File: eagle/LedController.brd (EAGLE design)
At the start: 64.8 x 34.3 mm, 20 parts, among them IC2 MEGA8-P, IC3 7805, Q1 16MHz, Q2 FDS8884, Q3 FDS8884, Q4 FDS8884, X1 2510-, X2 MKDSN1,5/4-5,08

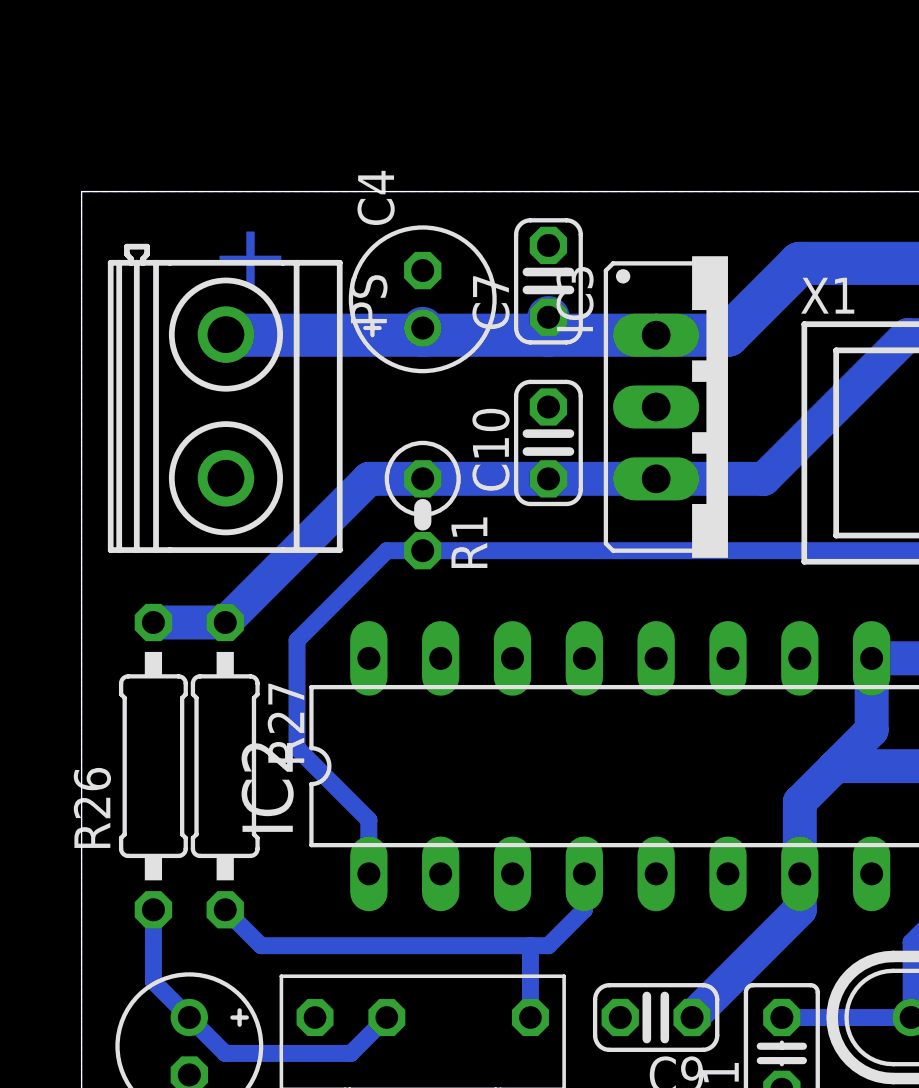
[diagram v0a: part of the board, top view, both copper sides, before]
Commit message: Add reverse polarity protection
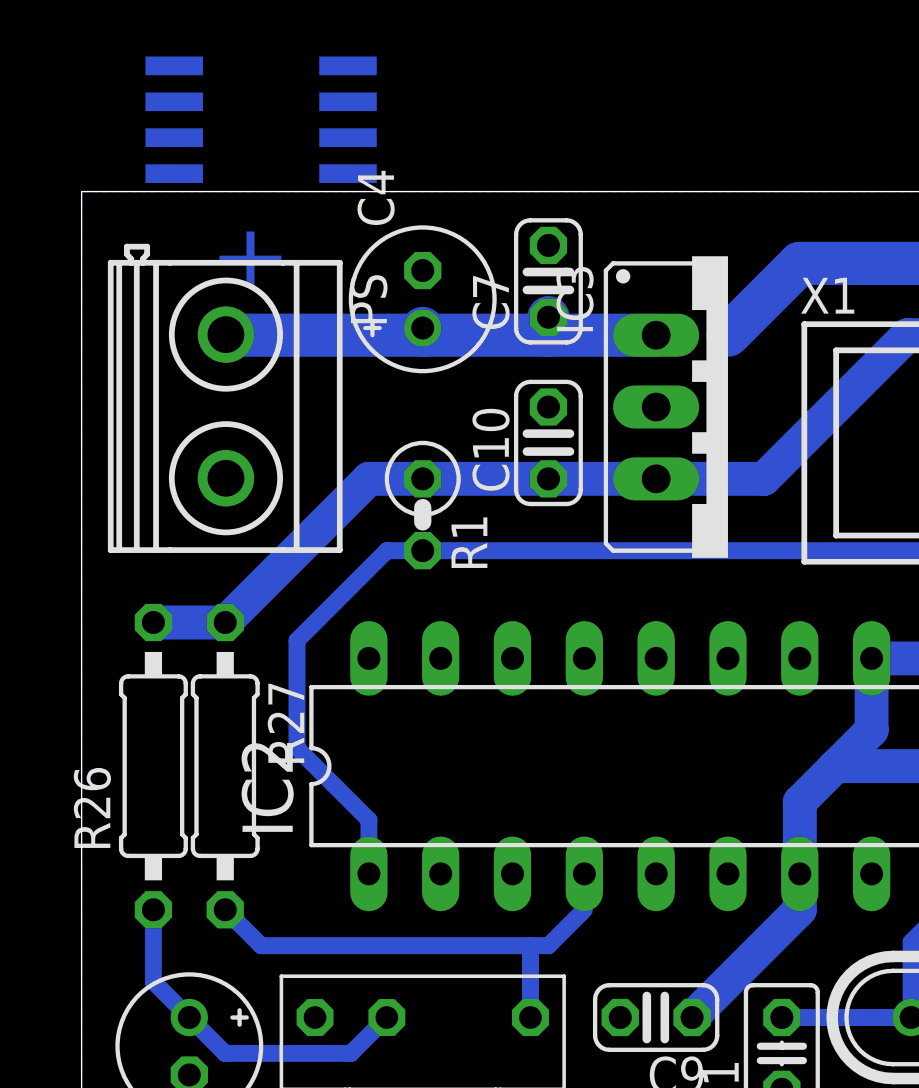
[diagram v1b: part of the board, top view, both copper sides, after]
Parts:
- added Q5: FDS8884, FDS8884:SO08
- renumbered U$1 to TSOP
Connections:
- net N$62 renamed IR
- new net N$8: PS.2, Q5.5, Q5.6, Q5.7, Q5.8
- net +12V: now also Q5.4
- net GND: now also Q5.1, Q5.2, Q5.3; no longer PS.2
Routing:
- net +12V: track 62.1 -> 59.6 mm
- net IR: track 17.6 -> 16.3 mm
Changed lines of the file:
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@@
 <element name="Q4" library="FDS8884" package="SO08" value="FDS8884" x="53.34" y="16.51" rot="MR90"/>
 <element name="X2" library="con-phoenix-508" package="MKDSN1,5/4-5,08" value="MKDSN1,5/4-5,08" x="59.69" y="13.335" rot="R90"/>
-<element name="U$1" library="TSOP1736" package="TSOP" value="TSOP" x="12.065" y="2.54"/>
+<element name="TSOP" library="TSOP1736" package="TSOP" value="TSOP" x="12.065" y="2.54"/>
 <element name="R1" library="rcl" package="0207/2V" value="10k" x="12.065" y="22.86" rot="R270"/>
+<element name="Q5" library="FDS8884" package="SO08" value="FDS8884" x="6.35" y="36.83" rot="MR270"/>
 </elements>
 <signals>
@@
 <contactref element="C10" pad="2"/>
 <contactref element="C4" pad="-"/>
-<contactref element="PS" pad="2"/>
 <contactref element="C15" pad="-"/>
 <contactref element="IC2" pad="22"/>
@@
 <contactref element="Q3" pad="2"/>
 <contactref element="Q3" pad="3"/>
-<contactref element="U$1" pad="GND"/>
+<contactref element="TSOP" pad="GND"/>
 <polygon width="0.4" layer="16" spacing="0.254" isolate="0.35">
 <vertex x="0" y="34.29"/>
@@
 <vertex x="64.77" y="34.29"/>
 </polygon>
+<contactref element="Q5" pad="1"/>
+<contactref element="Q5" pad="2"/>
+<contactref element="Q5" pad="3"/>
+<wire x1="9.4234" y1="37.465" x2="9.4234" y2="38.735" width="0" layer="19" extent="16-16"/>
+<wire x1="9.4234" y1="36.195" x2="9.4234" y2="37.465" width="0" layer="19" extent="16-16"/>
+<wire x1="12.065" y1="31.496" x2="9.4234" y2="36.195" width="0" layer="19" extent="16-16"/>
 </signal>
 <signal name="N$2">
@@
 <wire x1="35.56" y1="19.05" x2="40.64" y2="24.13" width="0.6" layer="16"/>
 </signal>
-<signal name="N$62">
+<signal name="IR">
 <contactref element="R27" pad="2"/>
-<contactref element="IC2" pad="4"/>
-<contactref element="U$1" pad="VO"/>
+<contactref element="TSOP" pad="VO"/>
 <wire x1="16.51" y1="7.62" x2="17.78" y2="8.89" width="0.6" layer="16"/>
-<wire x1="17.78" y1="8.89" x2="17.78" y2="10.16" width="0.6" layer="16"/>
 <wire x1="5.08" y1="8.89" x2="6.35" y2="7.62" width="0.6" layer="16"/>
 <wire x1="6.35" y1="7.62" x2="15.875" y2="7.62" width="0.6" layer="16"/>
 <wire x1="15.875" y1="7.62" x2="15.875" y2="5.08" width="0.6" layer="16"/>
 <wire x1="15.875" y1="7.62" x2="16.51" y2="7.62" width="0.6" layer="16"/>
+<contactref element="IC2" pad="4"/>
+<wire x1="17.78" y1="8.89" x2="17.78" y2="10.16" width="0" layer="19" extent="16-16"/>
 </signal>
 <signal name="N$63">
 <contactref element="R26" pad="1"/>
 <contactref element="C15" pad="+"/>
-<contactref element="U$1" pad="VS"/>
+<contactref element="TSOP" pad="VS"/>
 <wire x1="3.81" y1="5.08" x2="2.54" y2="6.35" width="0.6" layer="16"/>
 <wire x1="2.54" y1="6.35" x2="2.54" y2="8.89" width="0.6" layer="16"/>
@@
 </signal>
 <signal name="+12V">
+<contactref element="X2" pad="4"/>
+<wire x1="22.86" y1="29.21" x2="25.4" y2="31.75" width="1.524" layer="16"/>
+<wire x1="25.4" y1="31.75" x2="50.8" y2="31.75" width="1.524" layer="16"/>
+<wire x1="59.665" y1="22.885" x2="59.665" y2="20.9339" width="1.524" layer="16"/>
+<wire x1="50.8" y1="31.75" x2="59.665" y2="22.885" width="1.524" layer="16"/>
 <contactref element="PS" pad="1"/>
+<contactref element="Q5" pad="4"/>
 <contactref element="IC3" pad="IN"/>
 <contactref element="C7" pad="1"/>
 <contactref element="C4" pad="+"/>
-<contactref element="X2" pad="4"/>
-<wire x1="20.32" y1="29.21" x2="22.86" y2="29.21" width="1.524" layer="16"/>
-<wire x1="22.86" y1="29.21" x2="25.4" y2="31.75" width="1.524" layer="16"/>
-<wire x1="25.4" y1="31.75" x2="50.8" y2="31.75" width="1.524" layer="16"/>
-<wire x1="5.105" y1="29.2311" x2="5.1261" y2="29.21" width="1.5" layer="16"/>
 <wire x1="5.1261" y1="29.21" x2="12.065" y2="29.21" width="1.524" layer="16"/>
 <wire x1="12.065" y1="29.21" x2="16.51" y2="29.21" width="1.524" layer="16"/>
@@
 <wire x1="16.51" y1="29.21" x2="20.32" y2="29.21" width="1.524" layer="16"/>
 <wire x1="12.065" y1="29.21" x2="12.065" y2="29.464" width="1.5" layer="16"/>
-<wire x1="59.665" y1="22.885" x2="59.665" y2="20.9339" width="1.524" layer="16"/>
-<wire x1="50.8" y1="31.75" x2="59.665" y2="22.885" width="1.524" layer="16"/>
+<wire x1="20.32" y1="29.21" x2="22.86" y2="29.21" width="0" layer="19" extent="16-16"/>
+<wire x1="5.105" y1="29.2311" x2="5.1261" y2="29.21" width="0" layer="19" extent="16-16"/>
+<wire x1="9.4234" y1="34.925" x2="12.065" y2="29.464" width="0" layer="19" extent="16-16"/>
 </signal>
 <signal name="+5V">
@@
 <wire x1="33.02" y1="21.59" x2="12.065" y2="21.59" width="0.6" layer="16"/>
 </signal>
+<signal name="N$8">
+<contactref element="PS" pad="2"/>
+<contactref element="Q5" pad="5"/>
+<contactref element="Q5" pad="6"/>
+<contactref element="Q5" pad="7"/>
+<contactref element="Q5" pad="8"/>
+<wire x1="3.2766" y1="37.465" x2="3.2766" y2="38.735" width="0" layer="19" extent="16-16"/>
+<wire x1="3.2766" y1="36.195" x2="3.2766" y2="37.465" width="0" layer="19" extent="16-16"/>
+<wire x1="3.2766" y1="34.925" x2="3.2766" y2="36.195" width="0" layer="19" extent="16-16"/>
+<wire x1="5.105" y1="24.1511" x2="3.2766" y2="34.925" width="0" layer="19" extent="16-16"/>
+</signal>
 </signals>

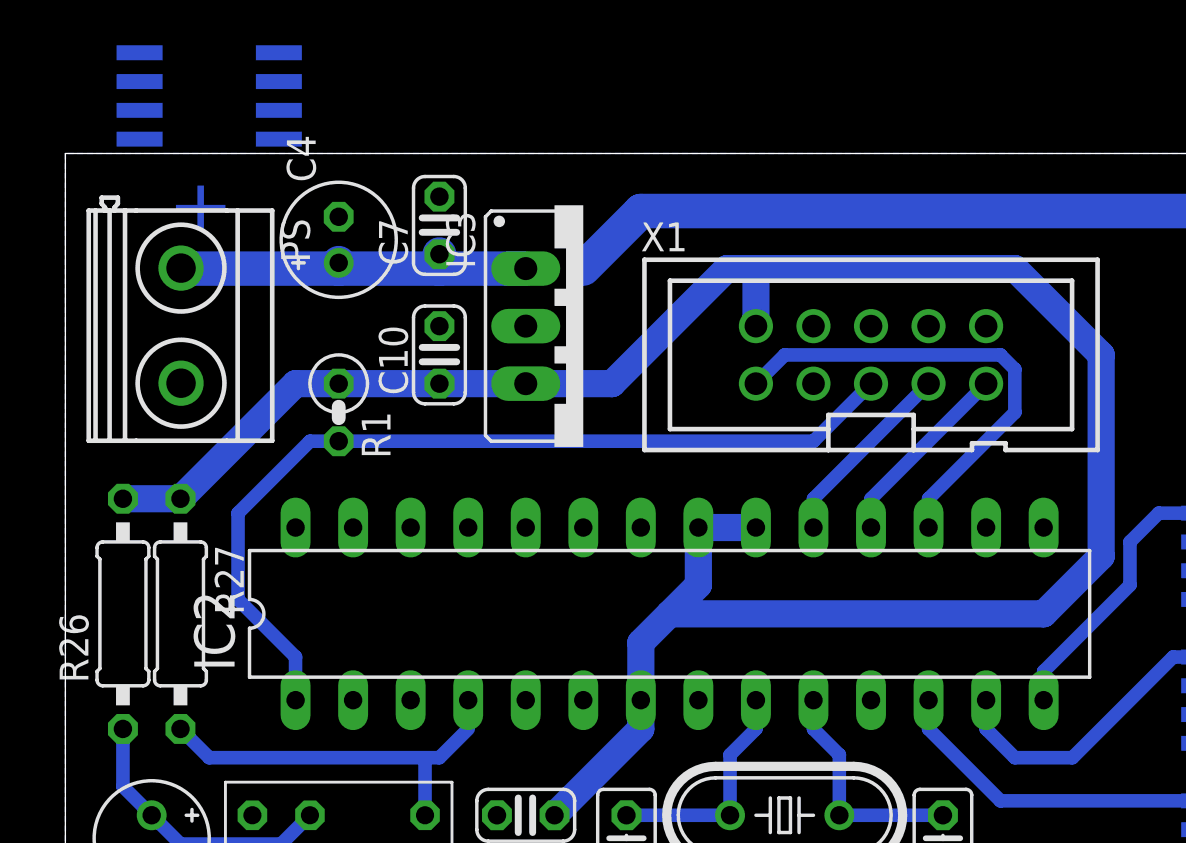
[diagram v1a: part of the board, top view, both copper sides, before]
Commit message: Changing Signal Names, split up into individual parts in schematic
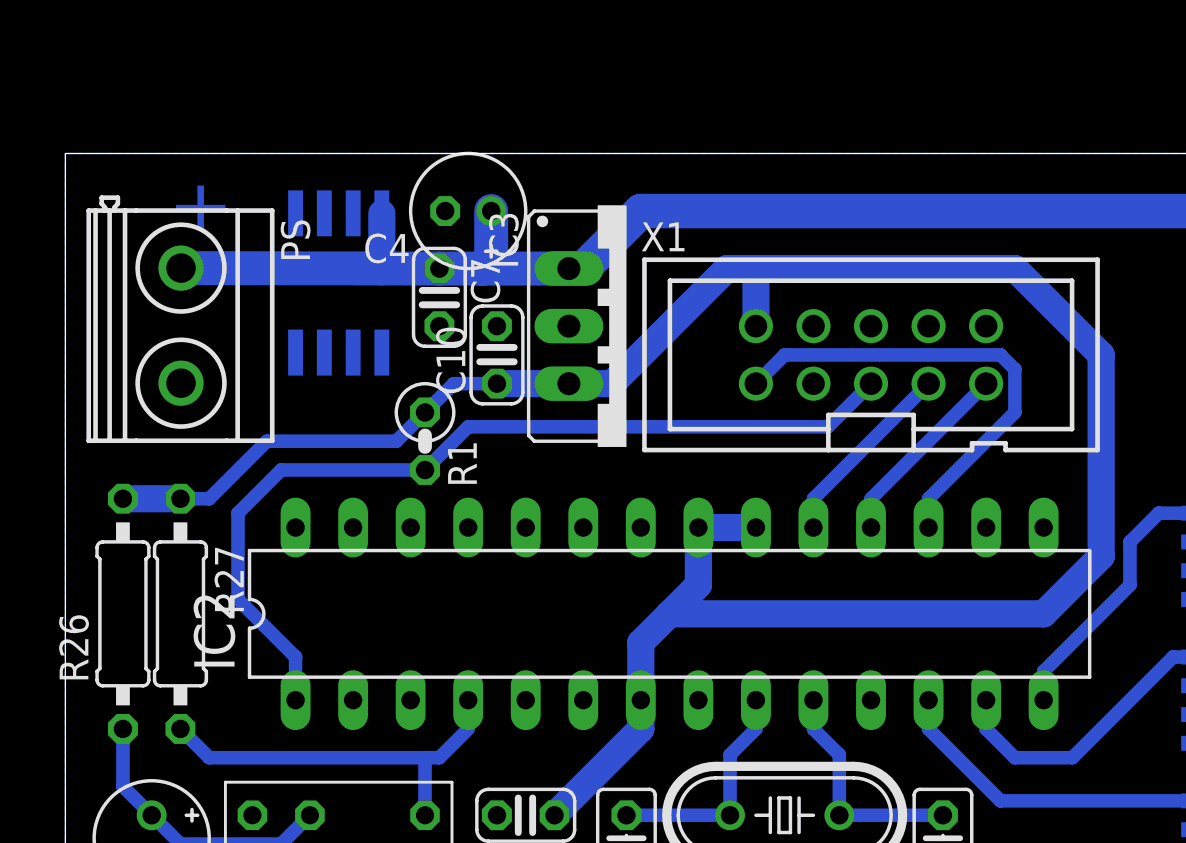
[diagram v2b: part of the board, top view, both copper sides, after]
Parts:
- moved Q5 10.0 mm to (12.1, 28.6), turned to 180 degrees
- moved C4 5.85 mm to (17.8, 31.8), turned to 180 degrees
- moved R1 4.02 mm to (15.9, 21.6)
- moved C7 3.17 mm to (16.5, 27.9), turned to 270 degrees
- moved C10 2.54 mm to (19.1, 25.4)
- moved IC3 1.91 mm to (24.8, 26.7)
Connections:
- net N$1 renamed ISP_MOSI
- net N$54 renamed ISP_CLK
- net N$7 renamed ISP_RESET
- net N$71 renamed ISP_MISO
- net RGB0 renamed PWM_R
- net RGB1 renamed PWM_G
- net RGB2 renamed PWM_B
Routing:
- net +12V: track 59.6 -> 66.4 mm
